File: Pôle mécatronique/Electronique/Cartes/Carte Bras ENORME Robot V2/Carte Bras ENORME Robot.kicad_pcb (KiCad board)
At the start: 2 copper layers, 44 x 70 mm, 31 parts, among them Q1 BC557, U1 MCP2551-I-P, U2 IRFZ44NPBF

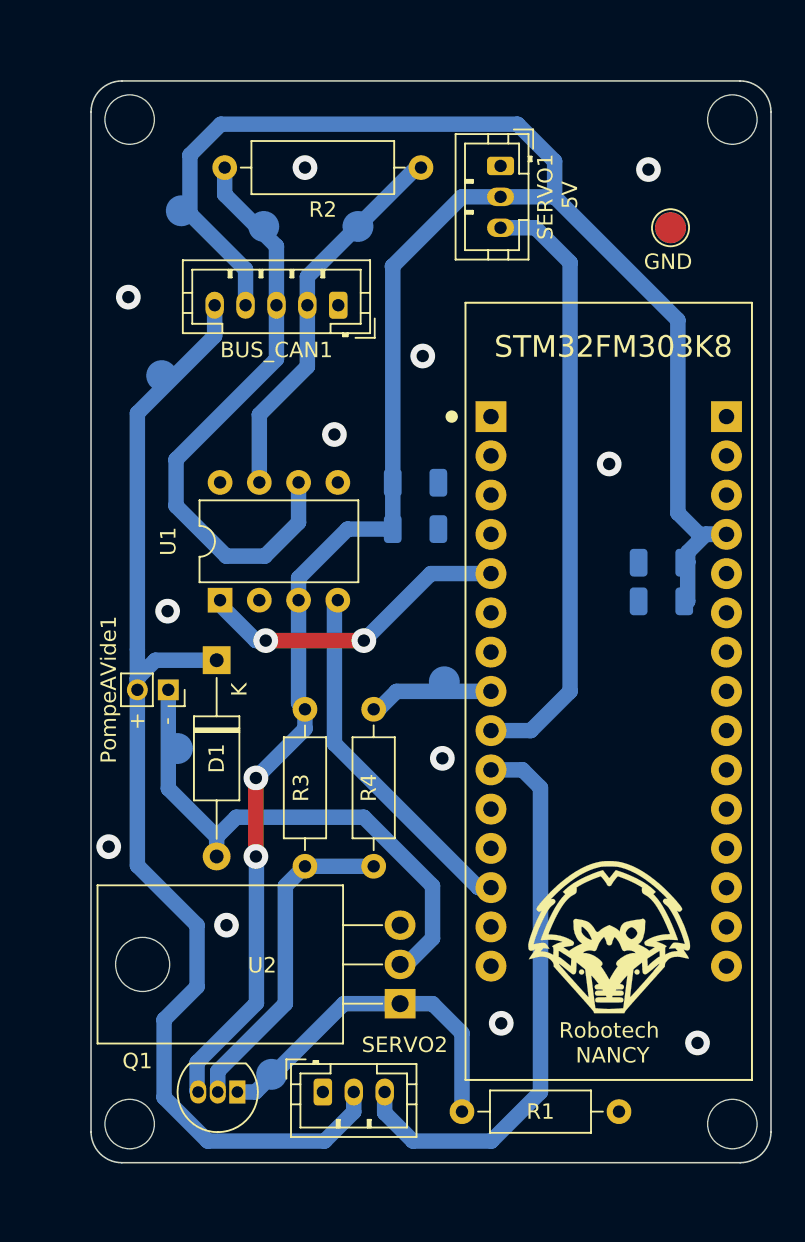
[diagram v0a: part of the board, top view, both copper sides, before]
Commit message: Update actionneur grand robot
Ajout d'une 2e empreinte avec détrompeur
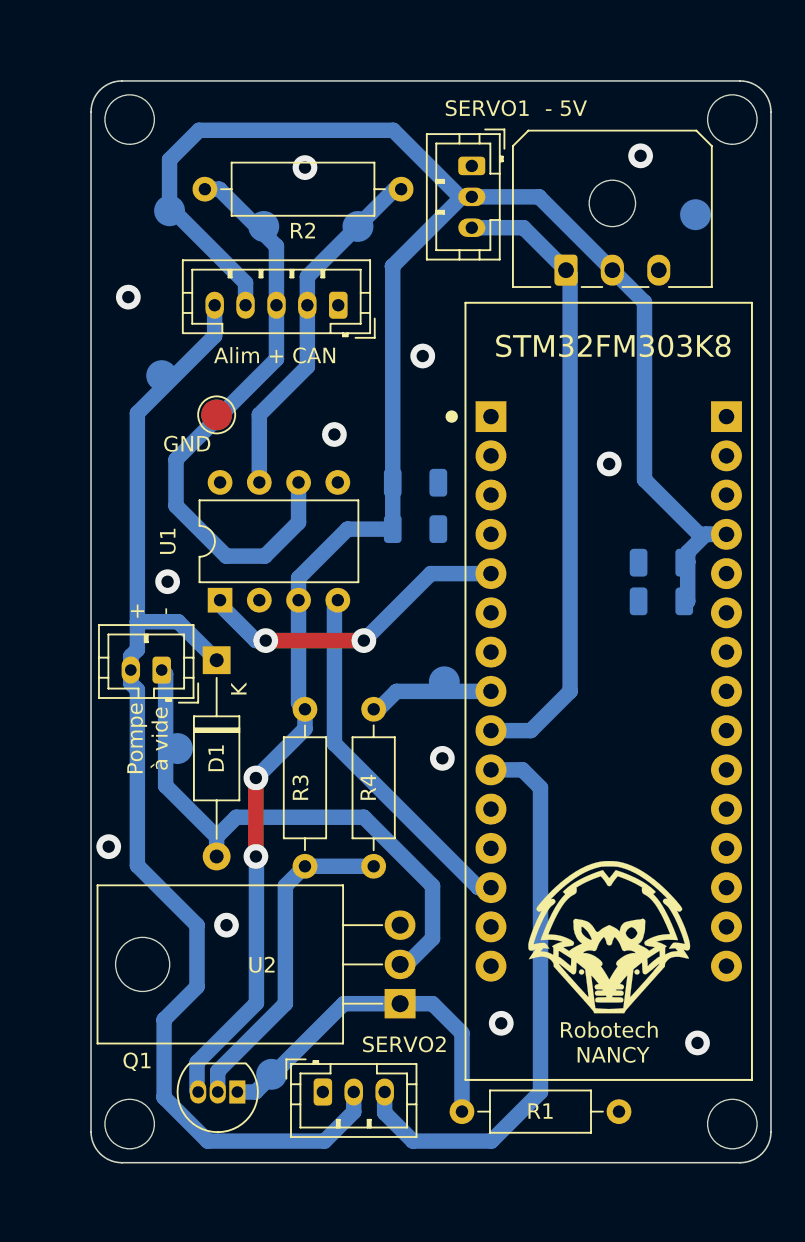
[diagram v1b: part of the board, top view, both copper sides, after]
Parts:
- added JS1: Molex_Micro-Fit_3.0_43650-0300_1x03_P3.00mm_Horizontal, Connector_Molex:Molex_Micro-Fit_3.0_43650-0300_1x03_P3.00mm_Horizontal, F.Cu at (173.7, 45.2)
- PompeAVide1: footprint Connector_PinSocket_2.00mm:PinSocket_1x02_P2.00mm_Vertical -> Connector_JST:JST_PH_B2B-PH-K_1x02_P2.00mm_Vertical
- moved TP1 31.8 mm to (151.1, 54.6)
- moved R2 1.90 mm to (163.1, 40.0)
- moved SERVO1 1.86 mm to (167.6, 38.5)
- moved ? 1.82 mm to (182.1, 41.7)
- moved PompeAVide1 1.35 mm to (147.6, 71.1), turned to 180 degrees
- moved TP3 0.76 mm to (148.1, 41.4)
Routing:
- net +5V: track 146.2 -> 140.3 mm
- net CAN_H: track 24.9 -> 23.0 mm
- net Net-(D1-Pad2): track 34.6 -> 36.1 mm
- net MOT1: track 39.4 -> 40.8 mm
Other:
- board text added: "- 5V"
- board text added: "Alim + CAN"
- board text added: "Pompe à vide"
